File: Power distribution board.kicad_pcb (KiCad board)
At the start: 2 copper layers, 29.2 x 94 mm, 20 parts, among them P1 CONN_1, P10 CONN_1, P2 CONN_1, P3 CONN_1, P4 CONN_1, P5 CONN_1, P6 CONN_1, P7 CONN_1, P8 CONN_1, P9 CONN_1

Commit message: Added image
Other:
- board text added: "+"
- board text added: "-"
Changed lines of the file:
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@@
     (area 16.434999 182.075001 58.982143 280.745001)
     (thickness 1.6)
-    (drawings 12)
+    (drawings 16)
     (tracks 28)
     (zones 0)
@@
     (visible_elements FFFFFFBF)
     (pcbplotparams
-      (layerselection 11042816)
+      (layerselection 296255488)
       (usegerberextensions false)
       (excludeedgelayer true)
@@
     )
   )
+  (gr_circle (center 33 277.55) (end 34.15 276.96) (layer F.SilkS) (width 0.2))
+  (gr_circle (center 25.39 277.55) (end 26.55 277) (layer F.SilkS) (width 0.2))
+  (gr_text - (at 25.4 277.5) (layer F.SilkS)
+    (effects (font (size 2 2) (thickness 0.3)))
+  )
+  (gr_text + (at 33 277.5) (layer F.SilkS)
+    (effects (font (size 2 2) (thickness 0.3)))
+  )
   (dimension 4 (width 0.25) (layer Dwgs.User)

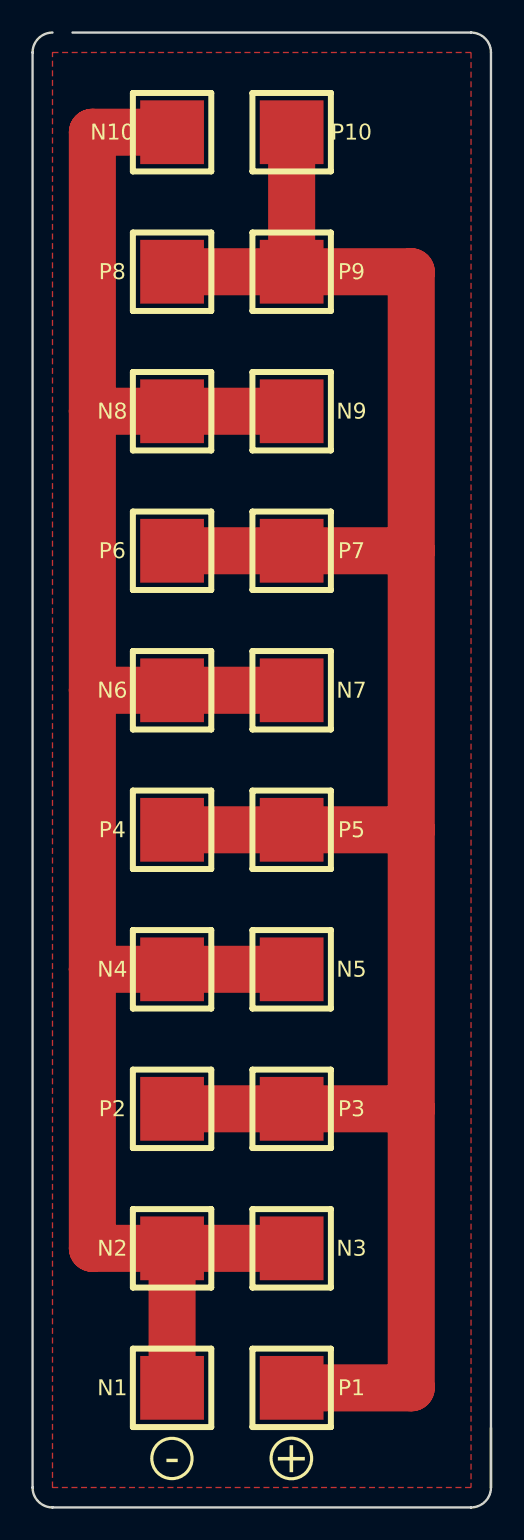
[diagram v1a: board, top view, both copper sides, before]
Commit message: Added plus and minus labels
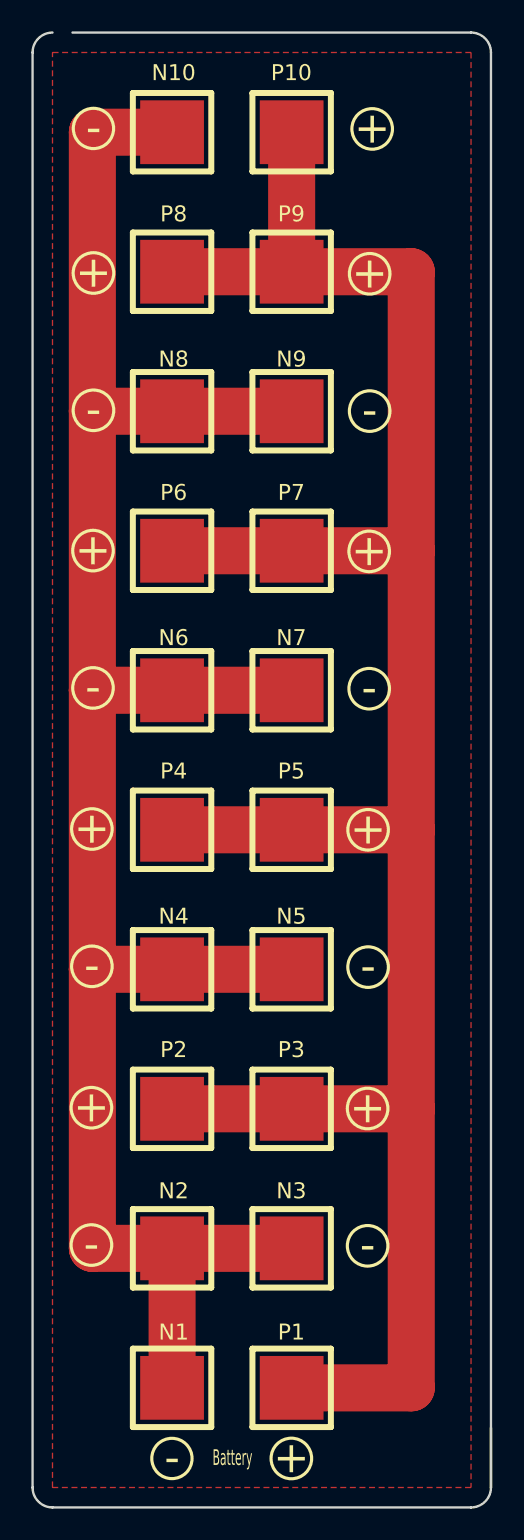
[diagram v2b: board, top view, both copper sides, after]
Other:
- board text added: "Battery"
